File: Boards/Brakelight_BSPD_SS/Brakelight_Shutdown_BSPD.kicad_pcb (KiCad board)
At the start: 2 copper layers, 59.2 x 76.3 mm, 71 parts, among them IC1 ATMEGA16M1, J2 MM_F_RA_20, J3 CONN_02X03, Q1 SSM3K333R, Q2 SSM3K333R, Q6 SSM3K333R, U1 SN74LVC1G08, U101 TPS560430YF, U2 MCP6001, U3 CAN_Transceiver, U4 MCP6001, U5 SN74LVC1G02, U6 SN74LVC1G02, U7 MCP6001, U8 SN74LVC1G32, Y1 Crystal_SMD

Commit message: Finished schematic
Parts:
- moved J3 160.2 mm to (47.8, 121.8)
- moved R3 132.5 mm to (59.1, 85.4), turned to 180 degrees
- moved D4 120.0 mm to (76.3, 108.8), turned to 0 degrees
- moved R18 119.5 mm to (74.4, 117.0), turned to 180 degrees
- moved C10 116.3 mm to (82.9, 123.8), turned to 270 degrees
- moved R17 115.9 mm to (77.5, 112.3), turned to 90 degrees
- moved U6 114.5 mm to (79.4, 122.6)
- moved Q1 114.0 mm to (70.1, 121.8), turned to 0 degrees
- moved Q2 114.0 mm to (74.2, 112.2), turned to 180 degrees
- moved R13 113.8 mm to (83.0, 119.4), turned to 90 degrees
- moved C101 113.5 mm to (70.4, 64.6)
- moved COUT101 113.5 mm to (82.6, 65.7)
- moved COUT102 113.5 mm to (81.5, 72.1)
- moved COUT103 113.5 mm to (82.6, 68.1)
- moved D101 113.5 mm to (65.6, 66.2)
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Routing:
- net VCC: track 113.4 -> 258.2 mm, vias 2 -> 4
- net GND: track 223.5 -> 148.2 mm, vias 29 -> 44
- net /LED_1: track 12.9 -> 67.8 mm
- net /MOSI: track 115.6 -> 64.0 mm, vias 6 -> 5
- net +12V: track 74.2 -> 22.8 mm, vias 1 -> 0
- net /MISO: track 112.4 -> 64.3 mm, vias 6 -> 5
- net /LED_2: track 11.1 -> 54.7 mm
- net /SCK: track 121.5 -> 77.9 mm, vias 8 -> 6
- net /RESET: track 106.5 -> 69.0 mm, vias 2 -> 6
- net /BSPD_Relay: track 49.1 -> 81.6 mm, vias 2 -> 0
- net /Brake_Pressure_Sense: track 37.5 -> 69.4 mm, vias 4 -> 5
- net /LED_3: track 9.44 -> 41.0 mm
- net /Cooling_Pump_LSD: track 21.9 -> 0.00 mm
- net /BSPD_Current_Sense: track 53.9 -> 38.3 mm
- net /Brakelight_Gate: track 54.2 -> 65.4 mm, vias 6 -> 2
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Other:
- board text added: "DNP"
- board text removed: "Crystal Clock"

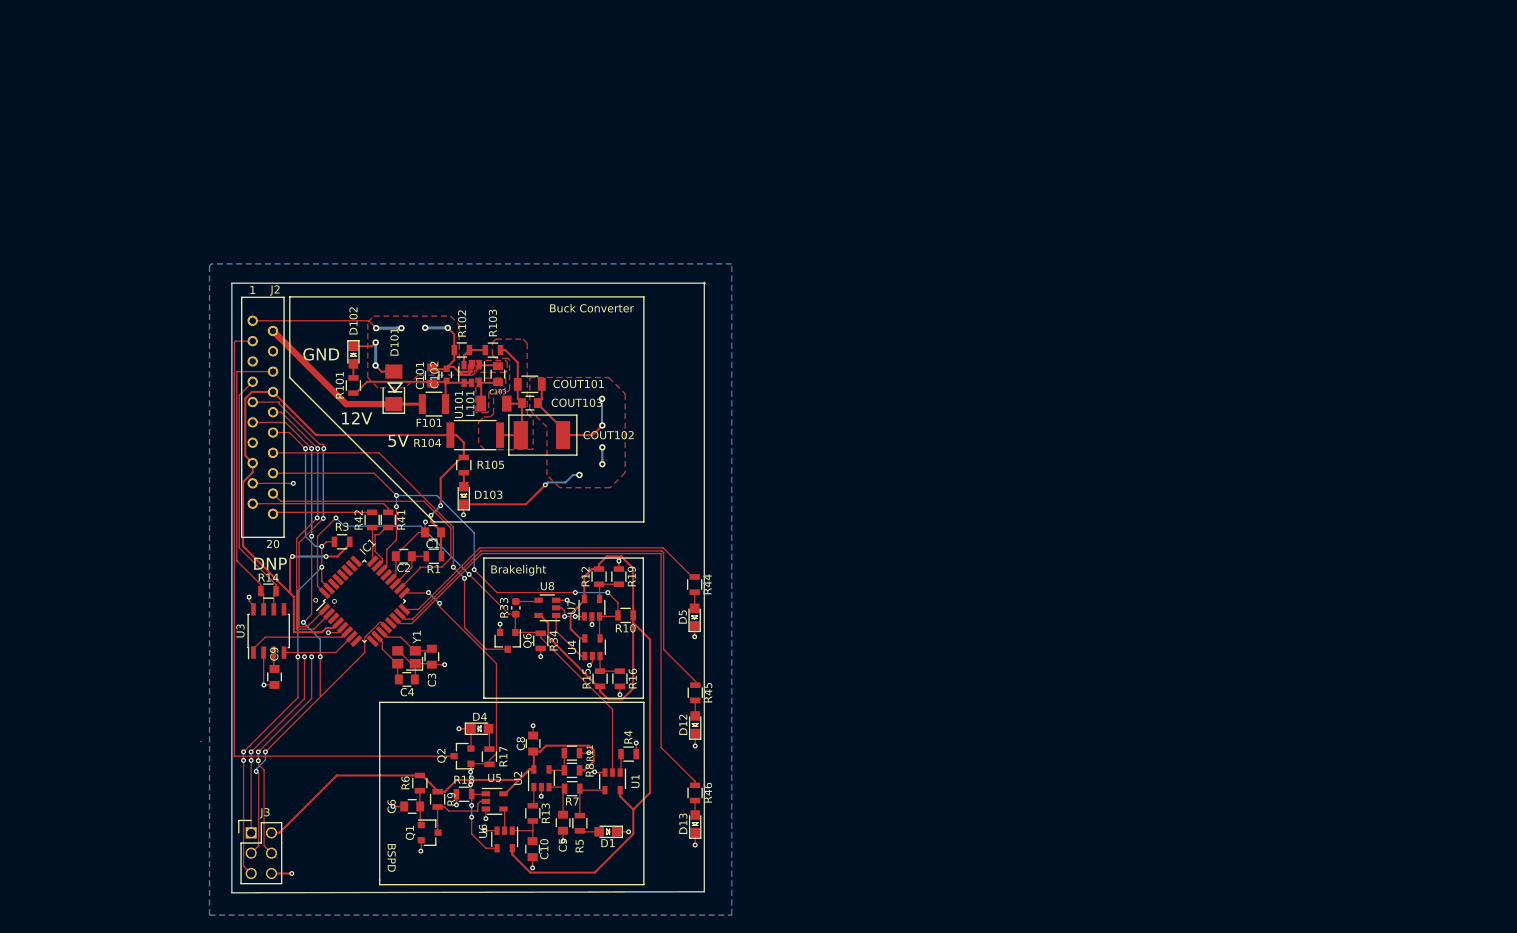
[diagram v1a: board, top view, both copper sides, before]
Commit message: Finished PCB layout
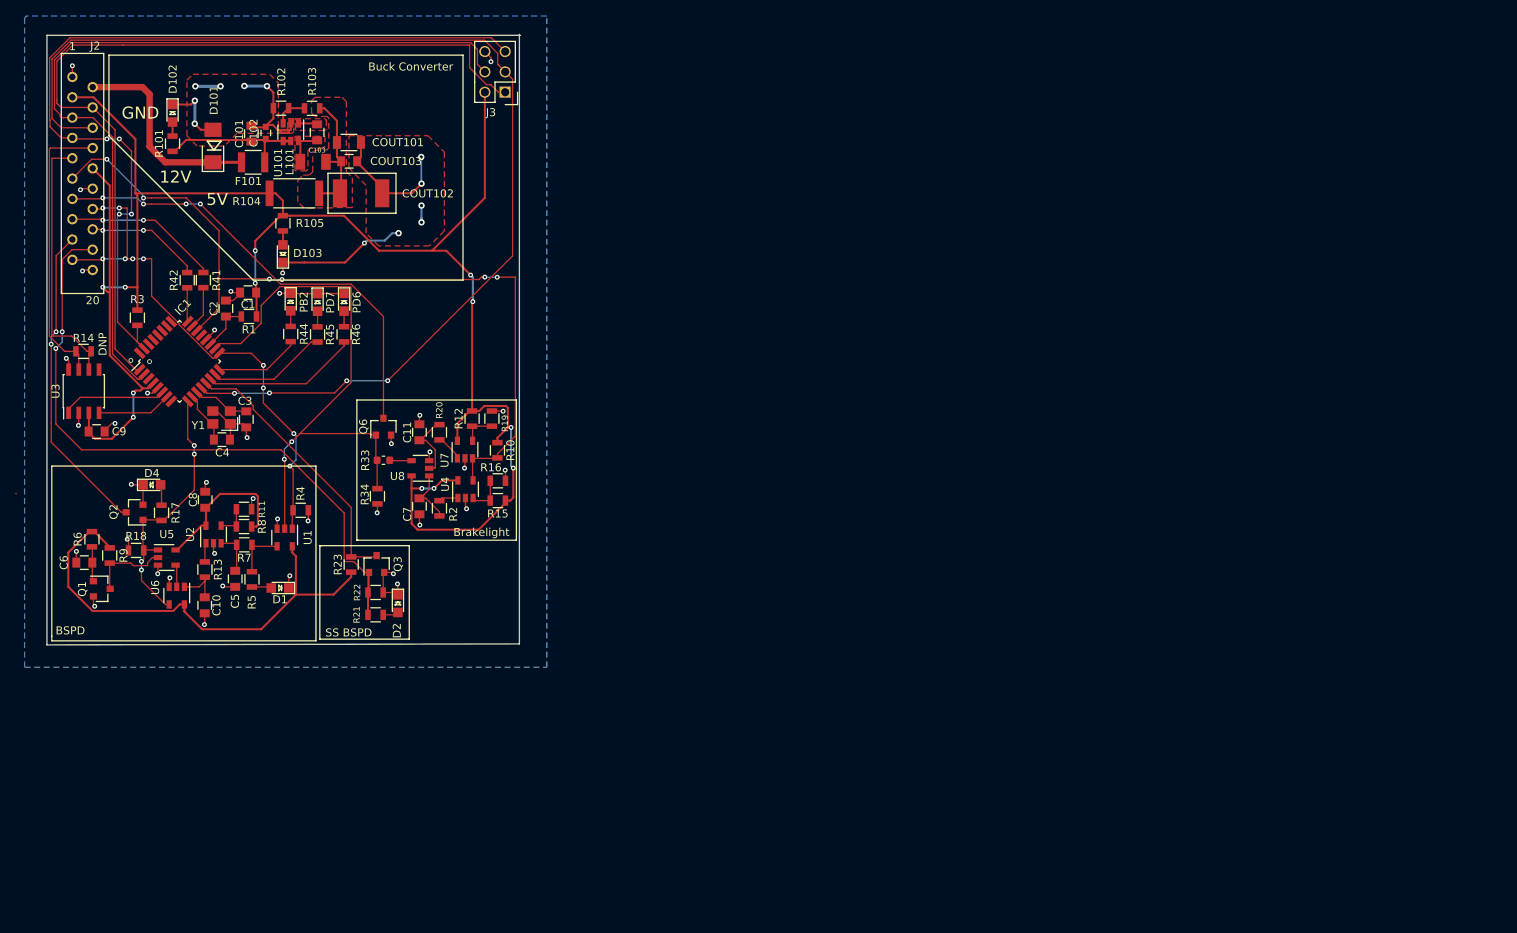
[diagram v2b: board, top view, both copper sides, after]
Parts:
- removed D12, D13, D5: LED_0805, footprints:LED_0805_OEM
- added C11: C_1uF, footprints:C_0805_OEM, F.Cu at (68.8, 71.7)
- added C7: C_1uF, footprints:C_0805_OEM, F.Cu at (68.8, 81.0)
- added D2: LED_0805, footprints:LED_0805_OEM, F.Cu at (66.1, 93.1)
- added PB2: LED_0805, footprints:LED_0805_OEM, F.Cu at (52.7, 55.4)
- added PD6: LED_0805, footprints:LED_0805_OEM, F.Cu at (59.4, 55.5)
- added PD7: LED_0805, footprints:LED_0805_OEM, F.Cu at (56.1, 55.5)
- added Q3: SSM3K333R, footprints:SOT-23F, F.Cu at (63.4, 88.2)
- added R2: R_10K, footprints:R_0805_OEM, F.Cu at (71.3, 81.2)
- added R20: R_10K, footprints:R_0805_OEM, F.Cu at (71.3, 71.7)
- added R21: R_10K, footprints:R_0805_OEM, F.Cu at (63.3, 94.5)
- added R22: R_100K, footprints:R_0805_OEM, F.Cu at (63.3, 91.7)
- added R23: R_10K, footprints:R_0805_OEM, F.Cu at (60.3, 88.2)
- moved J3 97.9 mm to (79.5, 29.2), turned to 180 degrees
- moved R46 72.2 mm to (59.4, 59.5), turned to 90 degrees
- moved R45 65.1 mm to (56.1, 59.5), turned to 90 degrees
- moved R44 59.4 mm to (52.7, 59.4), turned to 90 degrees
- moved R17 51.1 mm to (36.5, 81.8)
- moved R18 51.1 mm to (33.4, 86.5)
- moved R4 51.1 mm to (53.9, 81.5)
- moved U6 51.1 mm to (38.5, 92.1)
- moved C10 51.1 mm to (41.9, 93.3)
- moved C6 51.1 mm to (26.9, 88.0)
- moved D1 51.1 mm to (51.4, 91.2)
- moved Q1 51.1 mm to (29.1, 91.3)
- moved Q2 51.1 mm to (33.2, 81.7)
- moved R13 51.1 mm to (42.0, 88.9)
- moved R5 51.1 mm to (47.8, 90.1)
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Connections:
- net /LED_1 renamed /DEBUG_LED_1
- net /LED_2 renamed /DEBUG_LED_2
- net /LED_3 renamed /DEBUG_LED_3
- IC1 pad 13: Net-(IC1-Pad13) -> /SHUTDOWN_SENSE_BSPD_PIN
- IC1 pad 17: /BSPD_Relay_Sense -> /BSPD_CURRENT_SENSE
- IC1 pad 18: /BSPD_Current_Sense -> /BRAKELIGHT_GATE
- IC1 pad 22: /Brake_Pressure_Sense -> /BRAKE_PRESSURE_SENSE
- IC1 pad 30: /Cooling_Pump_LSD -> Net-(IC1-Pad30)
- IC1 pad 32: /Brakelight_Gate -> Net-(IC1-Pad32)
- IC1 pad 9: Net-(IC1-Pad9) -> /BSPD_RELAY_SENSE
- J2 pad 10: /MOSI -> VCC
- J2 pad 11: /SCK -> /BRAKE_PRESSURE_SENSE
- J2 pad 12: /RESET -> GND
- J2 pad 13: /Cooling_Pump_LSD -> /BRAKELIGHT_LSD
- J2 pad 14: /Brakelight_LSD -> /BSPD_CURRENT_SENSE
- J2 pad 15: VCC -> /RJ45_LED_G
- J2 pad 16: /Brake_Pressure_Sense -> /RJ45_LED_0
- J2 pad 17: GND -> /BSPD_RELAY_LSD
- J2 pad 18: /BSPD_Current_Sense -> /SHUTDOWN_SENSE_BSPD
- J2 pad 19: /RJ45_LED1 -> /BSPD_CURRENT_SENSE
- J2 pad 20: /RJ45_LED2 -> GND
- J2 pad 3: /BSPD_Relay -> VCC
- J2 pad 4: Net-(J2-Pad4) -> /MISO
- J2 pad 5: Net-(J2-Pad5) -> /MOSI
- J2 pad 6: /CAN_high -> /SCK
- J2 pad 7: /CAN_low -> /RESET
- J2 pad 8: VCC -> /CAN_HIGH
- J2 pad 9: /MISO -> /CAN_LOW
- Q2 pad 1: /BSPD_Relay_Sense -> /BSPD_RELAY_SENSE
- Q2 pad 3: /BSPD_Relay -> /BSPD_RELAY_LSD
- Q6 pad 1: /Brakelight_Gate -> /BRAKELIGHT_GATE
- Q6 pad 3: /Brakelight_LSD -> /BRAKELIGHT_LSD
- R10 pad 2: /Brake_Pressure_Sense -> /BRAKE_PRESSURE_SENSE
- R14 pad 1: /CAN_high -> /CAN_HIGH
- R14 pad 2: /CAN_low -> /CAN_LOW
- R17 pad 1: /BSPD_Relay_Sense -> /BSPD_RELAY_SENSE
- R18 pad 1: /BSPD_Relay_Sense -> /BSPD_RELAY_SENSE
- R33 pad 1: /Brakelight_Gate -> /BRAKELIGHT_GATE
- R34 pad 1: /Brakelight_Gate -> /BRAKELIGHT_GATE
- R4 pad 2: /BSPD_Current_Sense -> /BSPD_CURRENT_SENSE
- R41 pad 1: /RJ45_LED1 -> /RJ45_LED_G
- R42 pad 2: /RJ45_LED2 -> /RJ45_LED_0
- U1 pad 1: /BSPD_Current_Sense -> /BSPD_CURRENT_SENSE
- U1 pad 2: /Brakelight_Gate -> /BRAKELIGHT_GATE
- U3 pad 6: /CAN_low -> /CAN_LOW
- U3 pad 7: /CAN_high -> /CAN_HIGH
- U4 pad 1: Net-(U4-Pad1) -> Net-(R2-Pad2)
- U4 pad 4: /Brake_Pressure_Sense -> /BRAKE_PRESSURE_SENSE
- U5 pad 1: /BSPD_Relay_Sense -> /BSPD_RELAY_SENSE
- U6 pad 4: /BSPD_Relay_Sense -> /BSPD_RELAY_SENSE
- U7 pad 1: Net-(U7-Pad1) -> Net-(R20-Pad2)
- U7 pad 3: /Brake_Pressure_Sense -> /BRAKE_PRESSURE_SENSE
- U8 pad 1: Net-(U4-Pad1) -> Net-(C7-Pad1)
- U8 pad 2: Net-(U7-Pad1) -> Net-(C11-Pad1)
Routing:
- net /BRAKE_PRESSURE_SENSE: track 0.00 -> 103.5 mm, vias 0 -> 6
- net /SHUTDOWN_SENSE_BSPD: track 0.00 -> 86.0 mm, vias 0 -> 2
- net /BSPD_Relay: track 81.6 -> 0.00 mm
- net /BRAKELIGHT_GATE: track 0.00 -> 71.5 mm, vias 0 -> 2
- net /Brake_Pressure_Sense: track 69.4 -> 0.00 mm, vias 5 -> 0
- net /BSPD_CURRENT_SENSE: track 0.00 -> 66.1 mm, vias 0 -> 10
- net /Brakelight_Gate: track 65.4 -> 0.00 mm, vias 2 -> 0
- net /SCK: track 77.9 -> 142.8 mm, vias 6 -> 4
- net /BRAKELIGHT_LSD: track 0.00 -> 57.8 mm, vias 0 -> 4
- net VCC: track 258.2 -> 313.6 mm, vias 4 -> 12
- net /DEBUG_LED_1: track 67.8 -> 19.4 mm
- net /Brakelight_LSD: track 46.0 -> 0.00 mm, vias 2 -> 0
- net /BSPD_Relay_Sense: track 45.5 -> 0.00 mm, vias 6 -> 0
- net /MISO: track 64.3 -> 106.5 mm, vias 5 -> 0
- net /MOSI: track 64.0 -> 104.9 mm, vias 5 -> 0
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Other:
- board text added: "SS BSPD"

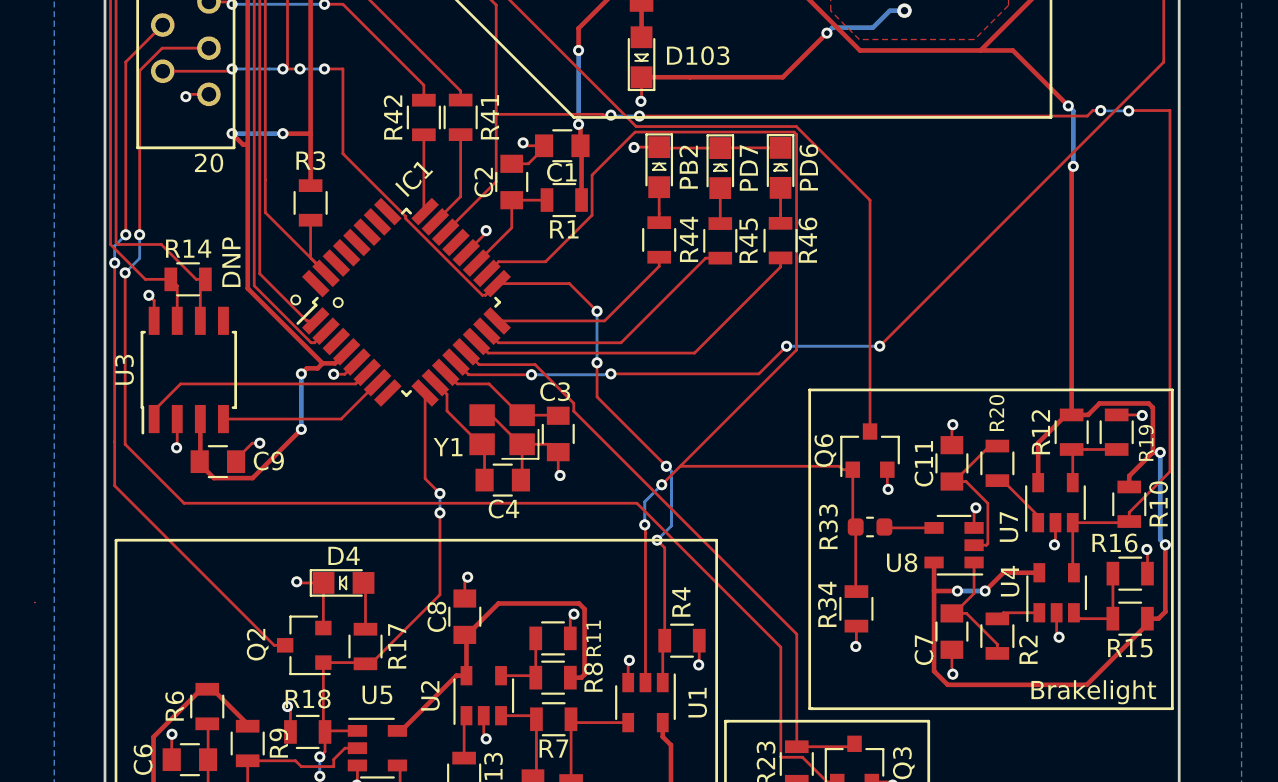
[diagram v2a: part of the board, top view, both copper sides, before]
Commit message: Updated layout from 11/2 design review
Added r_0 in before brakelight circuit. Added bypass capacitors
for op amps and OR gates.
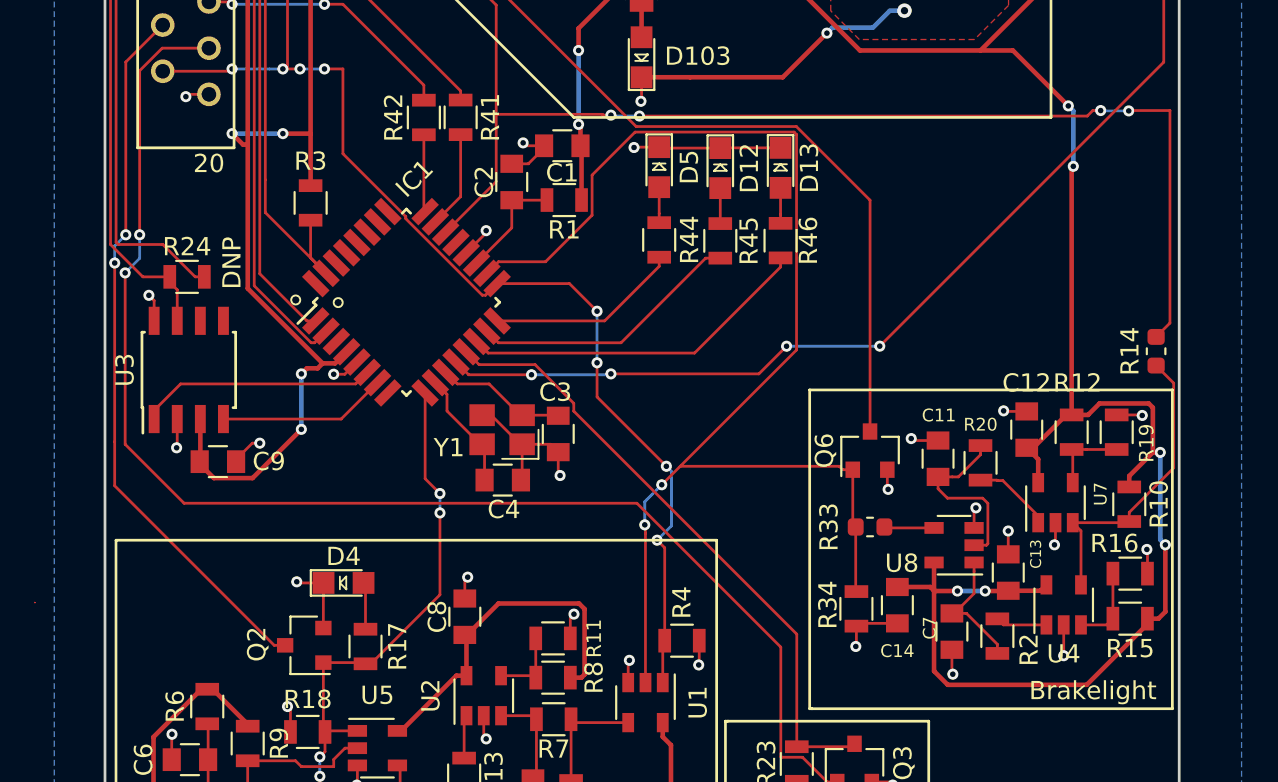
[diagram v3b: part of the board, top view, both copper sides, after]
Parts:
- added C12: C_0.1uF, footprints:C_0805_OEM, F.Cu at (72.9, 69.9)
- added C13: C_0.1uF, footprints:C_0805_OEM, F.Cu at (71.9, 77.7)
- added C14: C_0.1uF, footprints:C_0805_OEM, F.Cu at (65.8, 79.5)
- added R24: R_120_DNP, footprints:R_0805_OEM, F.Cu at (26.7, 61.5)
- R14: value R_200 -> R_0; footprint footprints:R_0805_OEM -> footprints:R_0603_1608Metric
- moved R14 53.4 mm to (80.0, 65.6), turned to 90 degrees
- moved R20 0.93 mm to (70.4, 71.7)
- moved C11 0.80 mm to (68.0, 71.5)
- moved U4 0.77 mm to (74.9, 79.5)
- renumbered PD7 to D12, PD6 to D13, PB2 to D5
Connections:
- net /BSPD_RELAY_SENSE renamed /BSPD_RELAY_INTENTION
- net /RJ45_LED_0 renamed /RJ45_LED_O
- R10 pad 2: /BRAKE_PRESSURE_SENSE -> Net-(R10-Pad2)
- R14 pad 1: /CAN_HIGH -> Net-(R10-Pad2)
- R14 pad 2: /CAN_LOW -> /BRAKE_PRESSURE_SENSE
- U4 pad 4: /BRAKE_PRESSURE_SENSE -> Net-(R10-Pad2)
- U7 pad 3: /BRAKE_PRESSURE_SENSE -> Net-(R10-Pad2)
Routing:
- net Net-(R10-Pad2): track 0.00 -> 16.7 mm
- net /BRAKE_PRESSURE_SENSE: track 103.5 -> 86.8 mm
- net GND: track 137.7 -> 143.3 mm, vias 50 -> 52
- net VCC: track 313.6 -> 316.5 mm
- net /CAN_LOW: track 33.2 -> 30.3 mm
- net Net-(C11-Pad1): track 8.80 -> 10.2 mm
- net Net-(R20-Pad2): track 3.42 -> 4.35 mm
